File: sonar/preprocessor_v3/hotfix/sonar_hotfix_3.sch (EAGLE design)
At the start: 26 parts, among them X1 BN35N61, X5 BN35N61, X9 BN35N61

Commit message: Implemented Mikes suggestions
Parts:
- removed C17, C19, C20: (no value), rcl:C-EUC0603
- removed U5: (no value), hotfix:LTC6240SO-8
- removed X9: BN35N61, ARVP:BN35N61
- added C5, C7, C8: (no value), rcl:C-EUC0603
- added U2: (no value), hotfix:LTC6240SO-8
- added X6: (no value), ARVP:BN35N61-HALF
- X2, X3: value (none) -> BN35N61; device ARVP:BN35N61-HALF -> ARVP:BN35N61
- X5: value BN35N61 -> (none); device ARVP:BN35N61 -> ARVP:BN35N61-HALF
- renumbered C18 to C6
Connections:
- net +5V: now also C10.1, C7.1, C8.1, C9.1, U2.V+; no longer C19.1, C20.1, C3.1, C4.1, U5.V+
- net -5V: now also C3.1, C4.1, C5.1, U2.V-; no longer C10.1, C17.1, C9.1, U5.V-
- net GND: now also C5.2, C7.2, C8.2, X6.2; no longer C17.2, C19.2, C20.2, X9.2
- net N$10: now also U3.-IN, U3.OUT, X6.1; no longer U5.-IN, U5.OUT, X4.1
- net N$2: now also X4.1; no longer X2.1
- net N$5: now also U2.+IN, X2.1; no longer U3.+IN, X5.1
- net N$6: now also U2.-IN, U2.OUT, X5.1; no longer U3.-IN, U3.OUT, X3.1
- net N$9: now also U3.+IN, X3.1; no longer U5.+IN, X9.1
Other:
- moved on the sheet: C10, C11, C12, C2, C3, C4, C9, U3, X2, X3, X4, X5

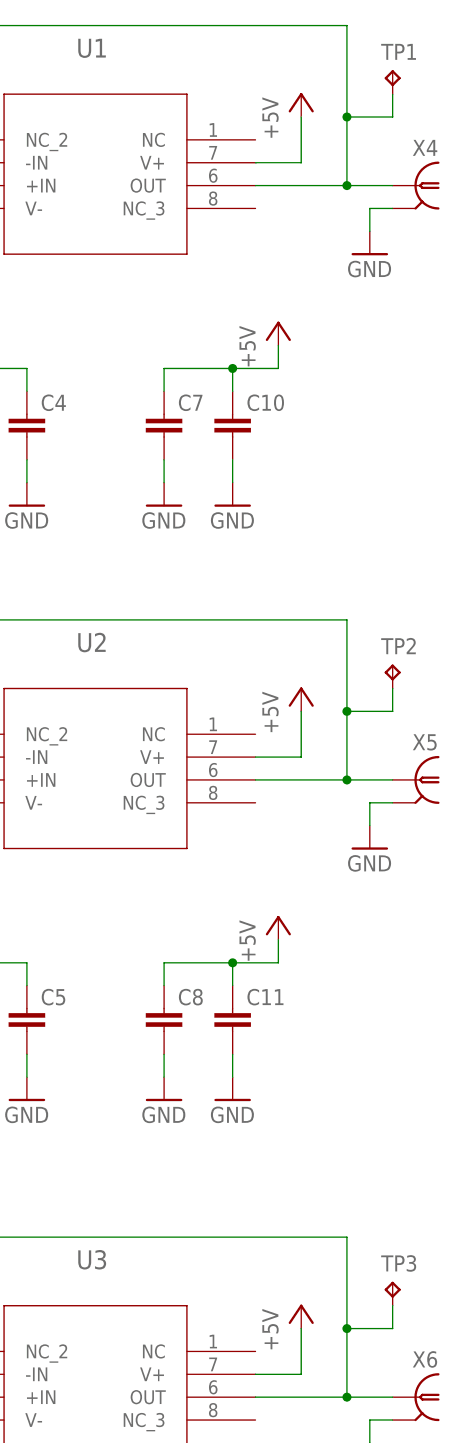
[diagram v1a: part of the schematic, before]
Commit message: Added CAM files; Changed power trace layout; Renamed test pads
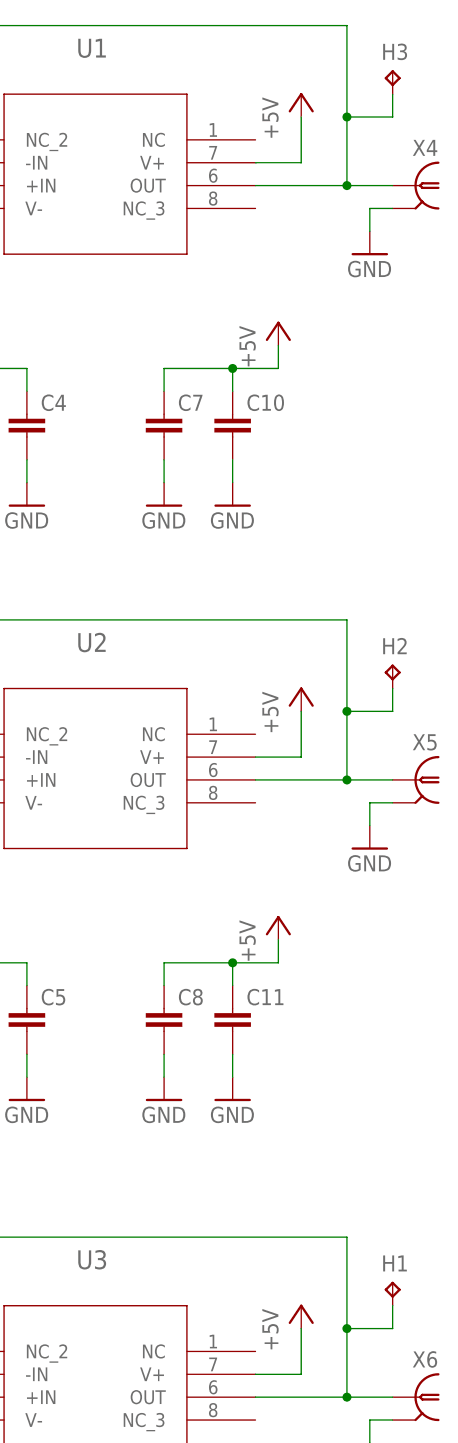
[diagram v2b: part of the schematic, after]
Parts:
- renumbered TP1 to H3, TP2 to H2, TP3 to H1
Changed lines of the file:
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@@
 <part name="X5" library="ARVP" deviceset="BN35N61-HALF" device=""/>
 <part name="X6" library="ARVP" deviceset="BN35N61-HALF" device=""/>
-<part name="TP1" library="testpad" library_urn="urn:adsk.eagle:library:385" deviceset="TP" device="B2,54" package3d_urn="urn:adsk.eagle:package:27948/1"/>
-<part name="TP2" library="testpad" library_urn="urn:adsk.eagle:library:385" deviceset="TP" device="B2,54" package3d_urn="urn:adsk.eagle:package:27948/1"/>
-<part name="TP3" library="testpad" library_urn="urn:adsk.eagle:library:385" deviceset="TP" device="B2,54" package3d_urn="urn:adsk.eagle:package:27948/1"/>
+<part name="H3" library="testpad" library_urn="urn:adsk.eagle:library:385" deviceset="TP" device="B2,54" package3d_urn="urn:adsk.eagle:package:27948/1"/>
+<part name="H2" library="testpad" library_urn="urn:adsk.eagle:library:385" deviceset="TP" device="B2,54" package3d_urn="urn:adsk.eagle:package:27948/1"/>
+<part name="H1" library="testpad" library_urn="urn:adsk.eagle:library:385" deviceset="TP" device="B2,54" package3d_urn="urn:adsk.eagle:package:27948/1"/>
 </parts>
 <sheets>
@@
 <instance part="X5" gate="G$1" x="35.56" y="-66.04" rot="MR0"/>
 <instance part="X6" gate="G$1" x="35.56" y="-134.62" rot="MR0"/>
-<instance part="TP1" gate="G$1" x="33.02" y="12.7"/>
-<instance part="TP2" gate="G$1" x="33.02" y="-53.34"/>
-<instance part="TP3" gate="G$1" x="33.02" y="-121.92"/>
+<instance part="H3" gate="G$1" x="33.02" y="12.7"/>
+<instance part="H2" gate="G$1" x="33.02" y="-53.34"/>
+<instance part="H1" gate="G$1" x="33.02" y="-121.92"/>
 </instances>
 <busses>
@@
 <junction x="27.94" y="0"/>
 <pinref part="X4" gate="G$1" pin="1"/>
-<pinref part="TP1" gate="G$1" pin="TP"/>
+<pinref part="H3" gate="G$1" pin="TP"/>
 <wire x1="33.02" y1="10.16" x2="33.02" y2="7.62" width="0.1524" layer="91"/>
 <wire x1="33.02" y1="7.62" x2="27.94" y2="7.62" width="0.1524" layer="91"/>
@@
 <junction x="27.94" y="-66.04"/>
 <pinref part="X5" gate="G$1" pin="1"/>
-<pinref part="TP2" gate="G$1" pin="TP"/>
+<pinref part="H2" gate="G$1" pin="TP"/>
 <wire x1="33.02" y1="-55.88" x2="33.02" y2="-58.42" width="0.1524" layer="91"/>
 <wire x1="33.02" y1="-58.42" x2="27.94" y2="-58.42" width="0.1524" layer="91"/>
@@
 <junction x="27.94" y="-134.62"/>
 <pinref part="X6" gate="G$1" pin="1"/>
-<pinref part="TP3" gate="G$1" pin="TP"/>
+<pinref part="H1" gate="G$1" pin="TP"/>
 <wire x1="33.02" y1="-124.46" x2="33.02" y2="-127" width="0.1524" layer="91"/>
 <wire x1="33.02" y1="-127" x2="27.94" y2="-127" width="0.1524" layer="91"/>
